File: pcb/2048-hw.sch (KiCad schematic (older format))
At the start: 101 parts

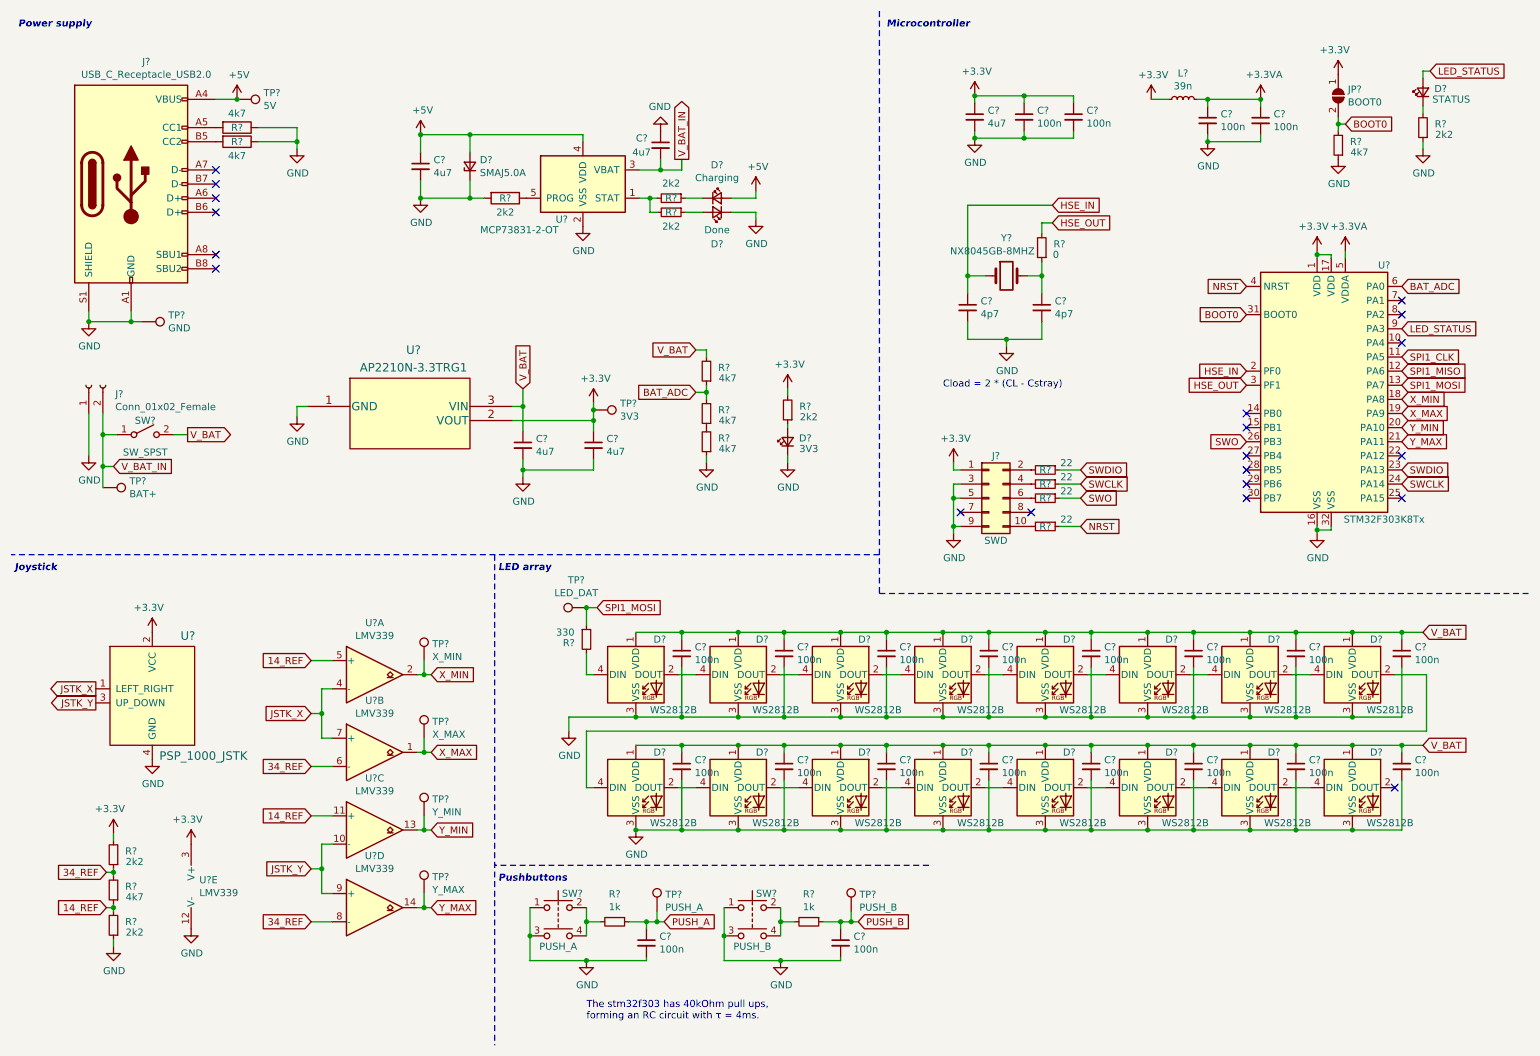
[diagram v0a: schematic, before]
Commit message: Annotate all components
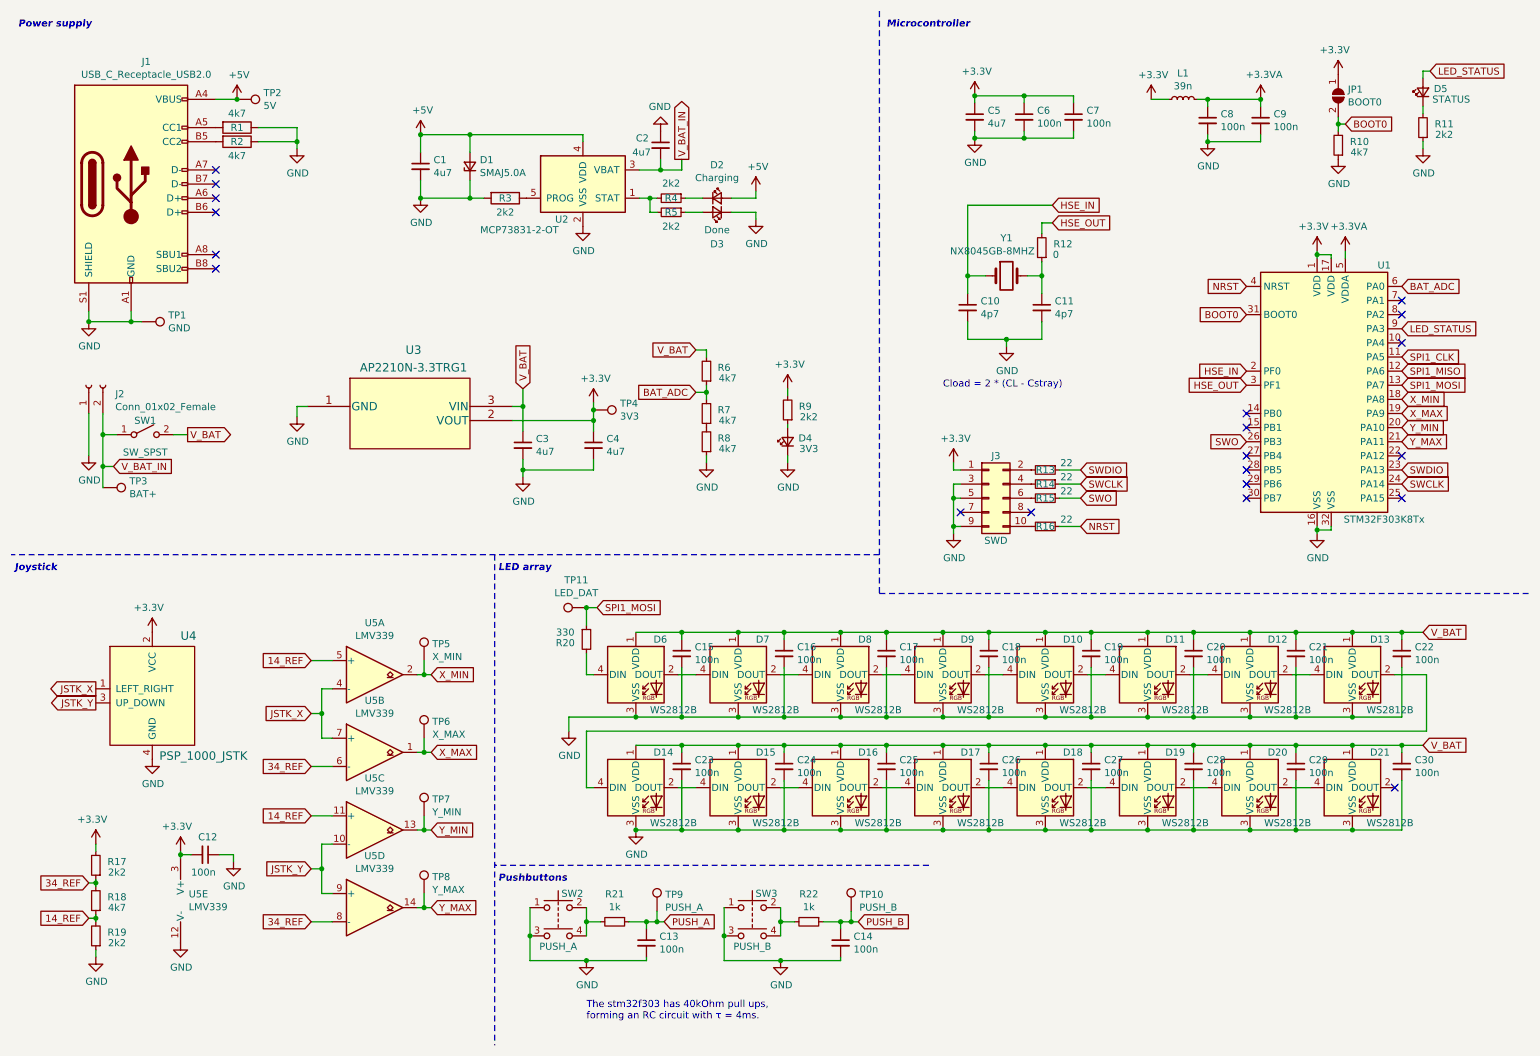
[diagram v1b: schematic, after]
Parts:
- added C12: 100n, symbol Device:C_Small
- gave numbers to parts that had none: 97
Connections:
- net +3V3: now also C12.2
- net GND: now also C12.1
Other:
- moved on the sheet: R17, R18, R19, U5E

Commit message: Make ERC pass
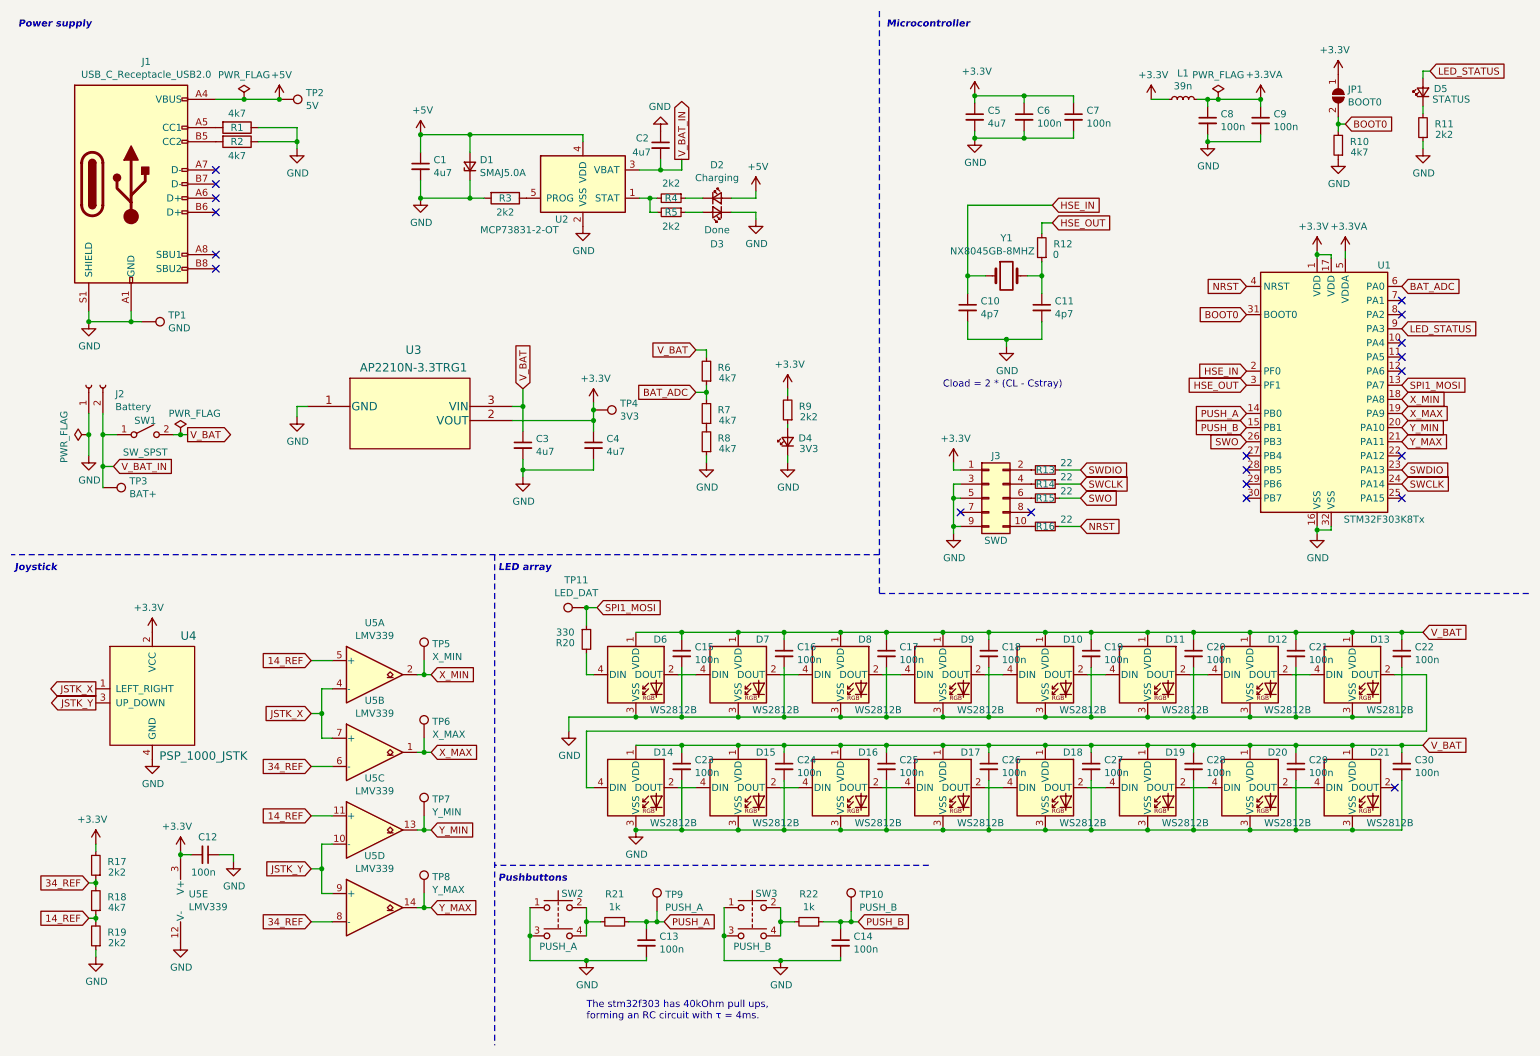
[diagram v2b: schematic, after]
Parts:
- J2: value Conn_01x02_Female -> Battery
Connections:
- net PUSH_A: now also U1.14 (PB0)
- net PUSH_B: now also U1.15 (PB1)
- net SPI1_CLK: no longer names the net of U1.11 (PA5)
- net SPI1_MISO: no longer names the net of U1.12 (PA6)
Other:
- moved on the sheet: TP2
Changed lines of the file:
@@
 L power:+5V #PWR0103
 U 1 1 5FEFEF31
-P 2075 1100
-F 0 "#PWR0103" H 2075 950 50  0001 C CNN
-F 1 "+5V" H 2090 1273 50  0000 C CNN
-F 2 "" H 2075 1100 50  0001 C CNN
-F 3 "" H 2075 1100 50  0001 C CNN
-	1    2075 1100
-	1    0    0    -1
-$EndComp
-Wire Wire Line
-	1925 1100 2075 1100
+P 2375 1100
+F 0 "#PWR0103" H 2375 950 50  0001 C CNN
+F 1 "+5V" H 2390 1273 50  0000 C CNN
+F 2 "" H 2375 1100 50  0001 C CNN
+F 3 "" H 2375 1100 50  0001 C CNN
+	1    2375 1100
+	1    0    0    -1
+$EndComp
 $Comp
 L power:GND #PWR0104
@@
 $EndComp
 Wire Wire Line
-	1025 3325 1025 3625
+	1025 3325 1025 3475
 Wire Wire Line
 	1125 3475 1125 3700
@@
 	1125 3325 1125 3475
 Wire Wire Line
-	1625 3475 1725 3475
+	1625 3475 1675 3475
 Wire Wire Line
 	1125 3475 1225 3475
@@
 P 1025 3125
 F 0 "J2" V 963 2937 50  0000 R CNN
-F 1 "Conn_01x02_Female" V 872 2937 50  0000 R CNN
+F 1 "Battery" V 872 2937 50  0000 R CNN
 F 2 "" H 1025 3125 50  0001 C CNN
 F 3 "~" H 1025 3125 50  0001 C CNN
@@
 	8950 1100 8950 1150
 Wire Wire Line
-	9325 1100 8950 1100
+	9325 1100 9025 1100
 Wire Wire Line
 	9325 1400 9325 1350
@@
 NoConn ~ 9225 3725
 NoConn ~ 9225 3625
-NoConn ~ 9225 3425
-NoConn ~ 9225 3325
 Text GLabel 10325 2425 2    50   Input ~ 0
 BAT_ADC
@@
 Text GLabel 10325 3125 2    50   Input ~ 0
 SPI1_MOSI
-Text GLabel 10325 3025 2    50   Input ~ 0
-SPI1_MISO
-Text GLabel 10325 2925 2    50   Input ~ 0
-SPI1_CLK
 Text GLabel 9225 3525 0    50   Input ~ 0
 SWO
@@
 L Connector:TestPoint TP2
 U 1 1 5FF27790
-P 2075 1100
-F 0 "TP2" V 2029 1288 50  0000 L CNN
-F 1 "5V" V 2120 1288 50  0000 L CNN
-F 2 "" H 2275 1100 50  0001 C CNN
-F 3 "~" H 2275 1100 50  0001 C CNN
-	1    2075 1100
+P 2375 1100
+F 0 "TP2" V 2329 1288 50  0000 L CNN
+F 1 "5V" V 2420 1288 50  0000 L CNN
+F 2 "" H 2575 1100 50  0001 C CNN
+F 3 "~" H 2575 1100 50  0001 C CNN
+	1    2375 1100
 	0    1    1    0
 $EndComp
-Connection ~ 2075 1100
 $Comp
 L Connector:TestPoint TP3
@@
 $EndComp
 $Comp
-L power:GND #PWR023
-U 1 1 60238A31
-P 2050 6500
-F 0 "#PWR023" H 2050 6250 50  0001 C CNN
-F 1 "GND" H 2055 6327 50  0000 C CNN
-F 2 "" H 2050 6500 50  0001 C CNN
-F 3 "" H 2050 6500 50  0001 C CNN
-	1    2050 6500
-	1    0    0    -1
-$EndComp
-$Comp
 L Device:C_Small C12
 U 1 1 60238D8D
@@
 Wire Wire Line
 	1675 6450 1750 6450
-Wire Wire Line
-	2050 6450 2050 6500
-Wire Wire Line
-	1950 6450 2050 6450
 Connection ~ 1675 6450
 Wire Wire Line
 	1675 6450 1675 6475
+Text GLabel 9225 3325 0    50   Input ~ 0
+PUSH_A
+Text GLabel 9225 3425 0    50   Input ~ 0
+PUSH_B
+$Comp
+L power:PWR_FLAG #FLG0101
+U 1 1 60308E93
+P 1675 3475
+F 0 "#FLG0101" H 1675 3550 50  0001 C CNN
+F 1 "PWR_FLAG" H 1775 3625 50  0000 C CNN
+F 2 "" H 1675 3475 50  0001 C CNN
+F 3 "~" H 1675 3475 50  0001 C CNN
+	1    1675 3475
+	1    0    0    -1
+$EndComp
+Connection ~ 1675 3475
+Wire Wire Line
+	1675 3475 1725 3475
+$Comp
+L power:PWR_FLAG #FLG0102
+U 1 1 6033C4C6
+P 2125 1100
+F 0 "#FLG0102" H 2125 1175 50  0001 C CNN
+F 1 "PWR_FLAG" H 2125 1273 50  0000 C CNN
+F 2 "" H 2125 1100 50  0001 C CNN
+F 3 "~" H 2125 1100 50  0001 C CNN
+	1    2125 1100
+	1    0    0    -1
+$EndComp
+Wire Wire Line
+	1925 1100 2125 1100
+Connection ~ 2375 1100
+Connection ~ 2125 1100
+Wire Wire Line
+	2125 1100 2375 1100
+$Comp
+L power:PWR_FLAG #FLG0103
+U 1 1 6038A345
+P 9025 1100
+F 0 "#FLG0103" H 9025 1175 50  0001 C CNN
+F 1 "PWR_FLAG" H 9025 1273 50  0000 C CNN
+F 2 "" H 9025 1100 50  0001 C CNN
+F 3 "~" H 9025 1100 50  0001 C CNN
+	1    9025 1100
+	1    0    0    -1
+$EndComp
+Connection ~ 9025 1100
+Wire Wire Line
+	9025 1100 8950 1100
+Wire Wire Line
+	2050 6500 2050 6450
+Wire Wire Line
+	2050 6450 1950 6450
+$Comp
+L power:GND #PWR0101
+U 1 1 603A72F9
+P 2050 6500
+F 0 "#PWR0101" H 2050 6250 50  0001 C CNN
+F 1 "GND" H 2055 6327 50  0000 C CNN
+F 2 "" H 2050 6500 50  0001 C CNN
+F 3 "" H 2050 6500 50  0001 C CNN
+	1    2050 6500
+	1    0    0    -1
+$EndComp
+$Comp
+L power:PWR_FLAG #FLG0104
+U 1 1 603AAADF
+P 1025 3475
+F 0 "#FLG0104" H 1025 3550 50  0001 C CNN
+F 1 "PWR_FLAG" H 825 3650 50  0000 L CNN
+F 2 "" H 1025 3475 50  0001 C CNN
+F 3 "~" H 1025 3475 50  0001 C CNN
+	1    1025 3475
+	0    -1   -1   0
+$EndComp
+Connection ~ 1025 3475
+Wire Wire Line
+	1025 3475 1025 3625
+NoConn ~ 10325 2925
+NoConn ~ 10325 3025
 $EndSCHEMATC

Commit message: Assign footprints
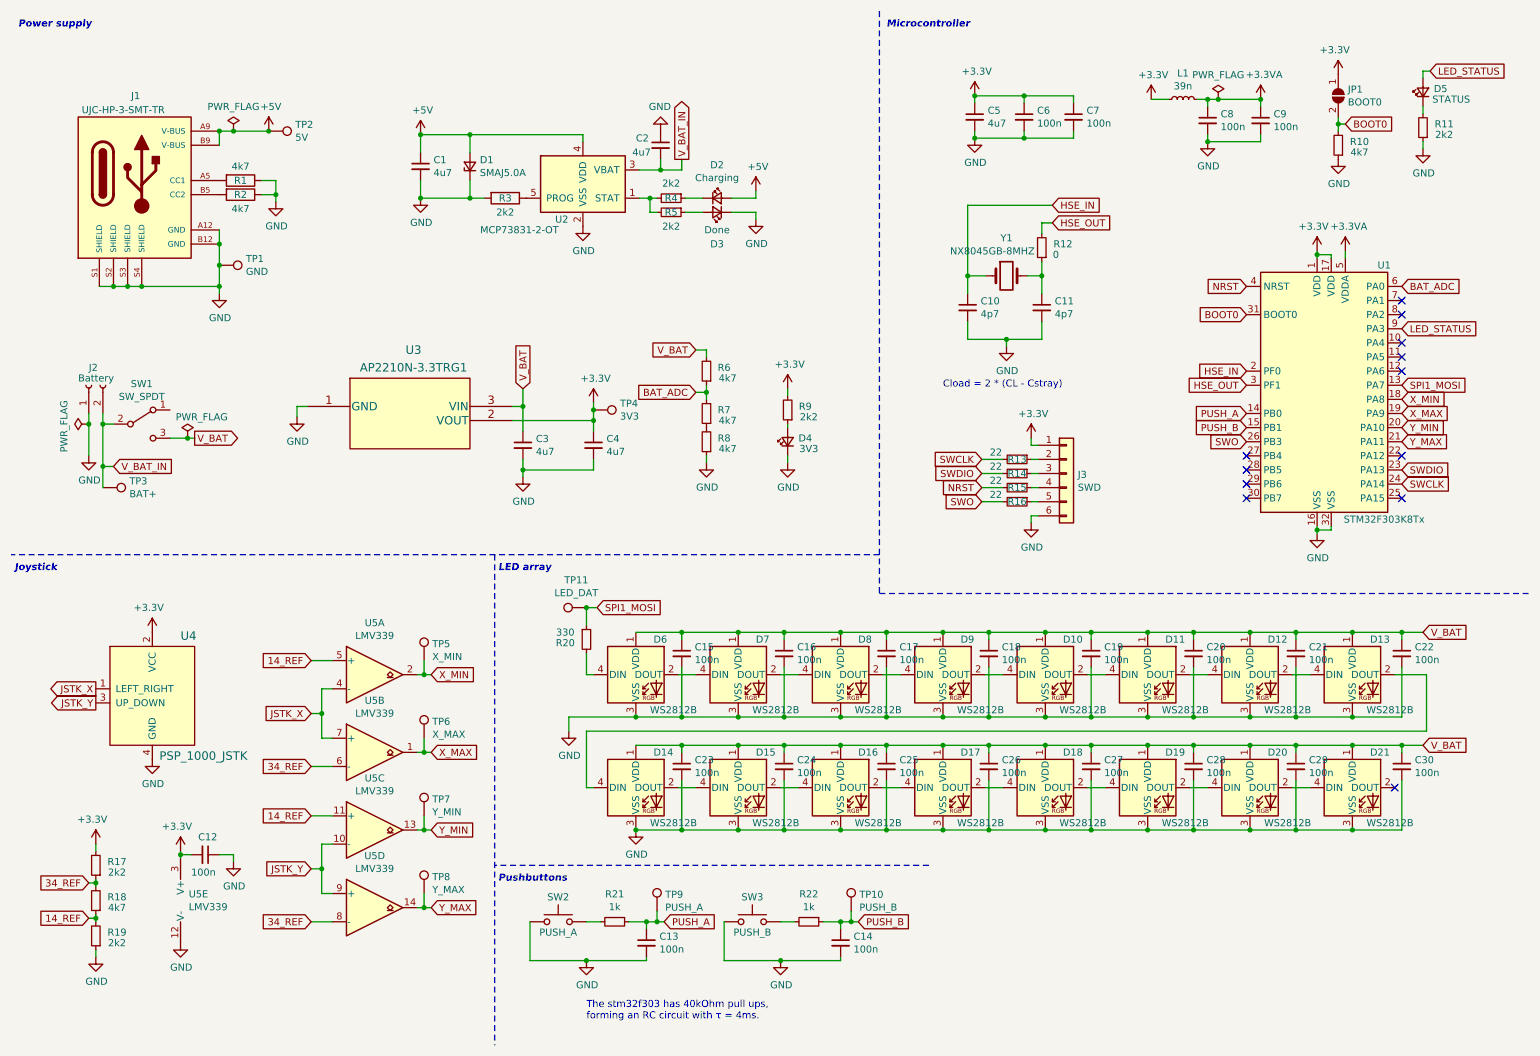
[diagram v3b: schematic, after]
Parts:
- removed J1: USB_C_Receptacle_USB2.0, symbol Connector:USB_C_Receptacle_USB2.0
- removed J3: SWD, symbol Connector_Generic:Conn_02x05_Odd_Even
- removed SW1: SW_SPST, symbol Switch:SW_SPST
- removed SW2: PUSH_A, symbol Switch:SW_Push_Dual
- removed SW3: PUSH_B, symbol Switch:SW_Push_Dual
- added J1: UJC-HP-3-SMT-TR, CUI_UJC-HP-3-SMT-TR:CUI_UJC-HP-3-SMT-TR, symbol UJC-HP-3-SMT-TR:UJC-HP-3-SMT-TR
- added J3: SWD, Connector_PinHeader_2.54mm:PinHeader_1x06_P2.54mm_Horizontal, symbol Connector_Generic:Conn_01x06
- added SW1: SW_SPDT, OS102011MS2QN1:SW_OS102011MS2QN1, symbol Switch:SW_SPDT
- added SW2: PUSH_A, Button_Switch_THT:SW_PUSH_6mm_H5mm, symbol Switch:SW_Push
- added SW3: PUSH_B, Button_Switch_THT:SW_PUSH_6mm_H5mm, symbol Switch:SW_Push
- C1, C10, C11, C12, C13, C14, C15, C16, C17, C18, C19, C2, C20, C21, C22, C23, C24, C25, C26, C27, C28, C29, C3, C30, C4, C5, C6, C7, C8, C9: footprint (none) -> Capacitor_SMD:C_0603_1608Metric_Pad1.08x0.95mm_HandSolder
- D1: footprint (none) -> Diode_SMD:D_SMA_Handsoldering
- D2, D3, D4, D5: footprint (none) -> LED_SMD:LED_0603_1608Metric_Pad1.05x0.95mm_HandSolder
- J2: footprint (none) -> Battery:BatteryHolder_Keystone_2460_1xAA
- JP1: footprint (none) -> Jumper:SolderJumper-2_P1.3mm_Open_RoundedPad1.0x1.5mm
- L1: footprint (none) -> Inductor_SMD:L_0603_1608Metric_Pad1.05x0.95mm_HandSolder
- R1, R10, R11, R12, R13, R14, R15, R16, R17, R18, R19, R2, R20, R21, R22, R3, R4, R5, R6, R7, R8, R9: footprint (none) -> Resistor_SMD:R_0603_1608Metric_Pad0.98x0.95mm_HandSolder
- TP1, TP10, TP11, TP2, TP3, TP4, TP5, TP6, TP7, TP8, TP9: footprint (none) -> TestPoint:TestPoint_THTPad_D2.0mm_Drill1.0mm
- U3: footprint SOT_3.3TRG1_DIO -> Package_TO_SOT_SMD:SOT-23
- U4: footprint (none) -> psp1000:JOYSTICK-PSP1000
- U5: footprint (none) -> Package_SO:SOIC-14_3.9x8.7mm_P1.27mm
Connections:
- net +3V3: now also J3.1 (Pin_1)
- net +5V: now also J1.A9 (V-BUS), J1.B9 (V-BUS)
- net GND: now also J1.A12 (GND), J1.B12 (GND), J1.S1 (SHIELD), J1.S2 (SHIELD), J1.S3 (SHIELD), J1.S4 (SHIELD), J3.6 (Pin_6), SW2.1, SW3.1
- net NRST: now also R15.2; no longer R16.1
- net SWCLK: now also R13.2; no longer R14.1
- net SWDIO: now also R14.2; no longer R13.1
- net SWO: now also R16.2; no longer R15.1
- net V_BAT: now also SW1.3 (C)
- net V_BAT_IN: now also SW1.2 (B)
- net at R1.2: now also J1.A5 (CC1)
- net at R2.2: now also J1.B5 (CC2)
- net at R21.2: now also SW2.2
- net at R22.2: now also SW3.2
- new net: J3.2 (Pin_2), R13.1
- new net: J3.3 (Pin_3), R14.1
- new net: J3.4 (Pin_4), R15.1
- new net: J3.5 (Pin_5), R16.1
- no-connect marks 20 -> 12
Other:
- moved on the sheet: R1, R13, R14, R15, R16, R2, TP1, TP2
